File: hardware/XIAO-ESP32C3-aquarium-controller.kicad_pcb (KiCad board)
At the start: 2 copper layers, 70 x 100 mm, 40 parts, among them J1 Conn_01x02, J2 Conn_01x07, J3 Conn_01x06, J4 Conn_01x03, J5 Conn_01x03, K1 SANYOU_SRD_Form_C, K2 SANYOU_SRD_Form_C, K3 SANYOU_SRD_Form_C, Q1 AO3400A, Q2 AO3400A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

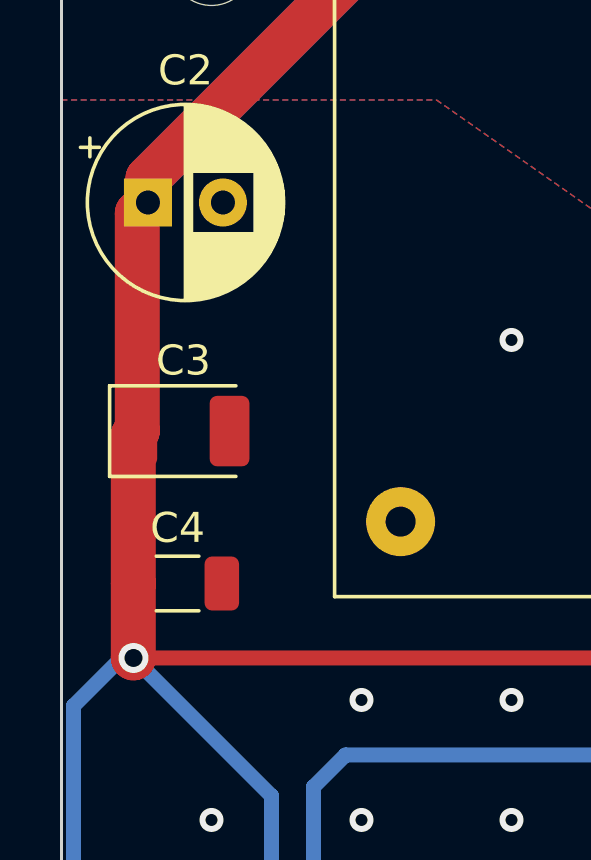
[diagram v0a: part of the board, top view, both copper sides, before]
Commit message: additional route for 5V input on B.Cu
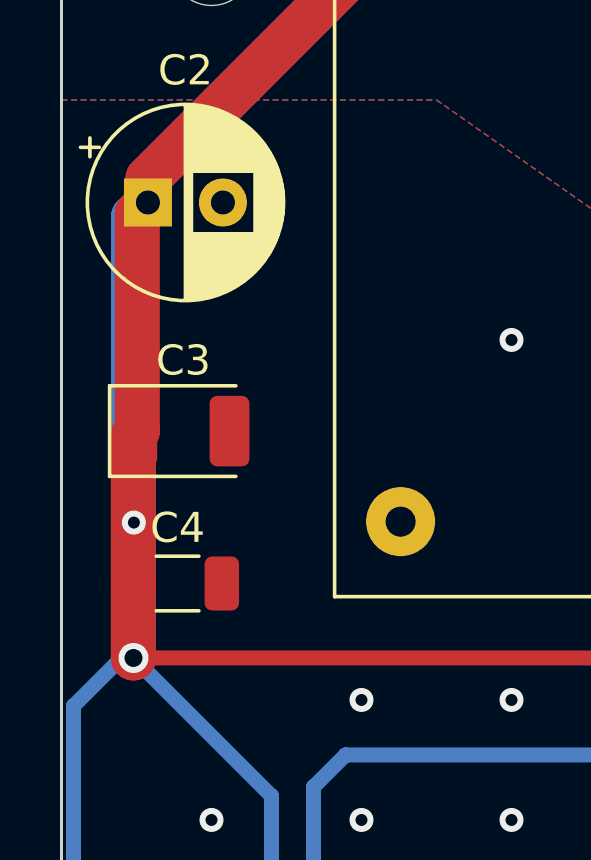
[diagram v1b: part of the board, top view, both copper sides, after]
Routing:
- net +5V: track 378.4 -> 393.8 mm, vias 1 -> 2
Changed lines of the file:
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@@
   (segment (start 60.909 80.955) (end 63.256 78.608) (width 0.5) (layer "F.Cu") (net 1))
   (via (at 34 57.6) (size 1) (drill 0.6) (layers "F.Cu" "B.Cu") (net 1))
+  (via (at 34.013 53.086) (size 0.8) (drill 0.4) (layers "F.Cu" "B.Cu") (net 1))
   (segment (start 38.6 62.2) (end 38.6 71.68875) (width 0.5) (layer "B.Cu") (net 1))
   (segment (start 34.48906 41.610939) (end 34.48906 42.41056) (width 1.5) (layer "B.Cu") (net 1))
   (segment (start 42.910939 30.24856) (end 42.910939 33.18906) (width 1.5) (layer "B.Cu") (net 1))
   (segment (start 68.502 72.518) (end 68.502 77.898) (width 0.5) (layer "B.Cu") (net 1))
+  (segment (start 34.013 53.086) (end 34 53.099) (width 1.5) (layer "B.Cu") (net 1))
+  (segment (start 34 53.099) (end 34 57.6) (width 1.5) (layer "B.Cu") (net 1))
   (segment (start 33.6 57.6) (end 32 59.2) (width 0.5) (layer "B.Cu") (net 1))
   (segment (start 72.802 84.474) (end 68.502 88.774) (width 0.5) (layer "B.Cu") (net 1))
@@
   (segment (start 32 119.8) (end 36.4 124.2) (width 0.5) (layer "B.Cu") (net 1))
   (segment (start 68.5 77.9) (end 68.5 80.172) (width 0.5) (layer "B.Cu") (net 1))
+  (segment (start 34.481621 42.418) (end 34 42.899621) (width 1.5) (layer "B.Cu") (net 1))
   (segment (start 72.802 100.634) (end 68.43 105.006) (width 0.5) (layer "B.Cu") (net 1))
   (segment (start 68.502 96.334) (end 72.802 100.634) (width 0.5) (layer "B.Cu") (net 1))
+  (segment (start 34 53.073) (end 34.013 53.086) (width 1.5) (layer "B.Cu") (net 1))
   (segment (start 42.910939 33.18906) (end 34.48906 41.610939) (width 1.5) (layer "B.Cu") (net 1))
   (segment (start 68.502 77.898) (end 68.5 77.9) (width 0.5) (layer "B.Cu") (net 1))
@@
   (segment (start 34 57.6) (end 33.6 57.6) (width 0.5) (layer "B.Cu") (net 1))
   (segment (start 32 59.2) (end 32 119.8) (width 0.5) (layer "B.Cu") (net 1))
+  (segment (start 34 42.899621) (end 34 53.073) (width 1.5) (layer "B.Cu") (net 1))
   (segment (start 68.502 88.774) (end 68.502 96.334) (width 0.5) (layer "B.Cu") (net 1))
   (segment (start 48.11 122.69) (end 48.11 121.717) (width 0.5) (layer "B.Cu") (net 1))

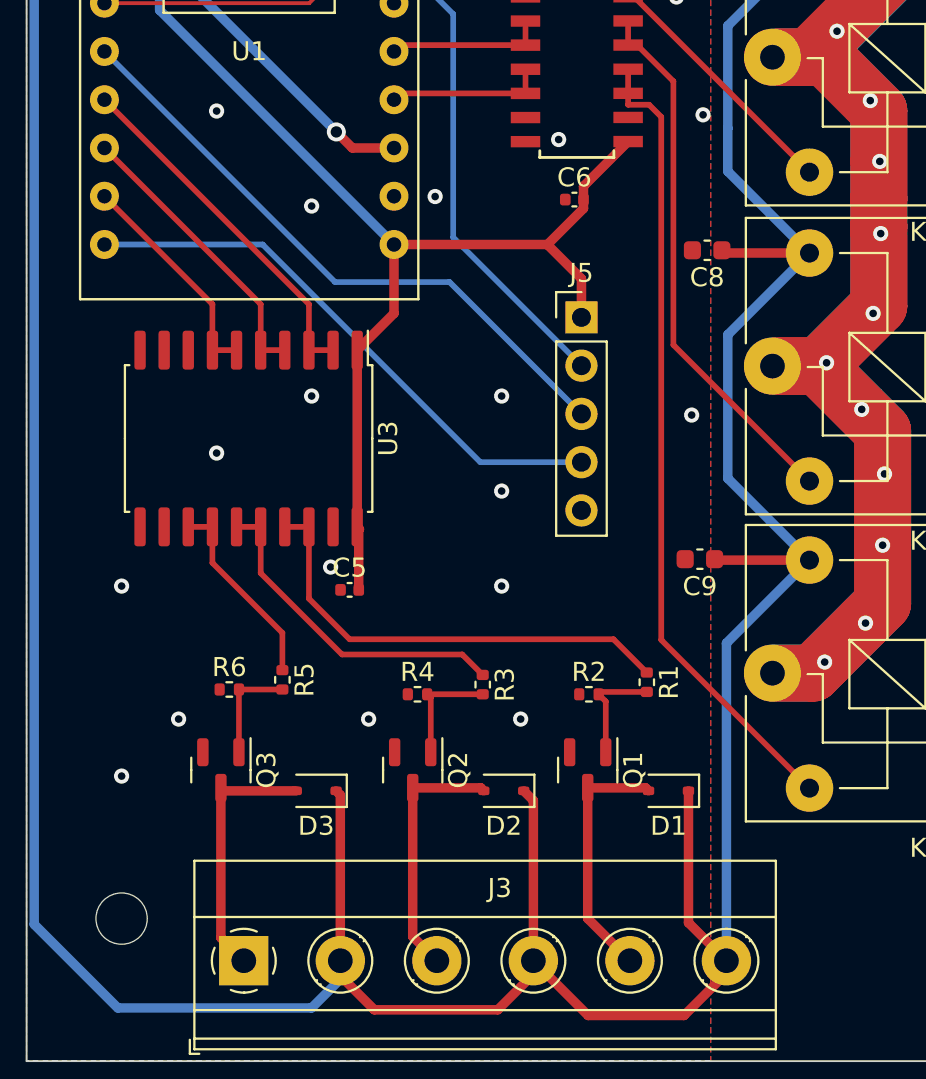
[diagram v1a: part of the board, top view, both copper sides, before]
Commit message: capacitor at mosfet
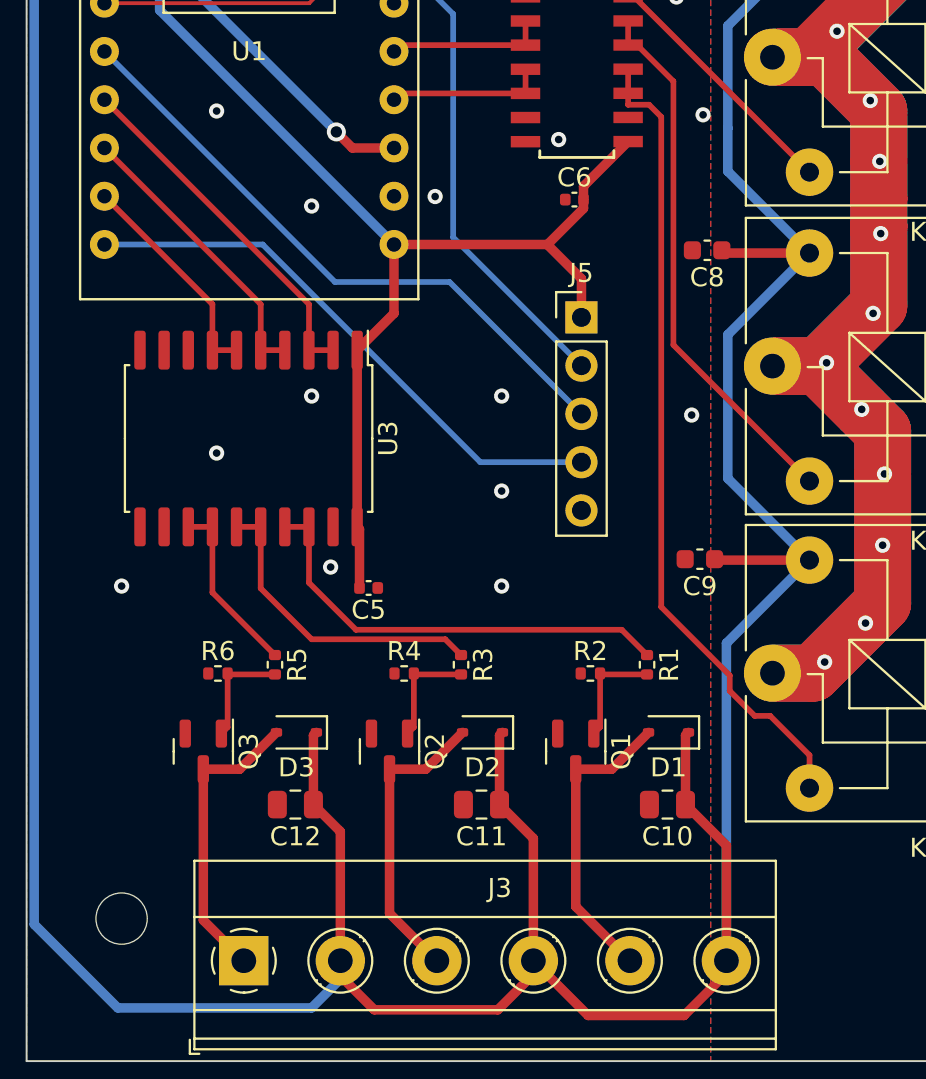
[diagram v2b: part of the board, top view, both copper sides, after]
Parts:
- added C10: 22uF, Capacitor_SMD:C_0805_2012Metric, F.Cu at (65.3, 113.5)
- added C11: 22uF, Capacitor_SMD:C_0805_2012Metric, F.Cu at (55.5, 113.5)
- added C12: 22uF, Capacitor_SMD:C_0805_2012Metric, F.Cu at (45.7, 113.5)
- moved D2 3.27 mm to (55.6, 109.7)
- moved D3 3.25 mm to (45.8, 109.7)
- moved D1 3.08 mm to (65.4, 109.7)
- moved Q2 1.57 mm to (50.7, 110.7)
- moved R3 1.55 mm to (54.5, 106.1)
- moved Q3 1.35 mm to (40.9, 110.7)
- moved R4 1.30 mm to (51.5, 106.6)
- moved Q1 1.17 mm to (60.5, 110.7)
- moved R2 1.10 mm to (61.3, 106.6)
- moved R6 1.03 mm to (41.7, 106.6)
- moved C5 1.00 mm to (49.6, 102.1), turned to 180 degrees
- moved R1 0.92 mm to (64.3, 106.1)
- moved R5 0.89 mm to (44.7, 106.1)
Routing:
- net +5V: track 393.8 -> 404.1 mm
- net /MosfetRelay1/Vout: track 13.3 -> 15.9 mm
- net /MosfetRelay2/Vout: track 13.4 -> 15.8 mm
- net /MosfetRelay3/Vout: track 13.6 -> 15.6 mm
- net /rel6: track 17.6 -> 16.5 mm
- net /rel7: track 10.3 -> 9.38 mm
- net /rel5: track 24.4 -> 23.6 mm
- net GND: vias 28 -> 24
